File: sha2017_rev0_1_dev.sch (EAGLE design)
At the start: 87 parts, among them IC1 AP7215, IC2 LM1117, IC3 CP210X_USB_UART, IC4 ESP32WROOM32, Q1 MMBT2222A, Q2 MMBT2222A, Q3 SI1304 BDL, SW100 MCMT5-F-V, X701 2908-05WB-MG

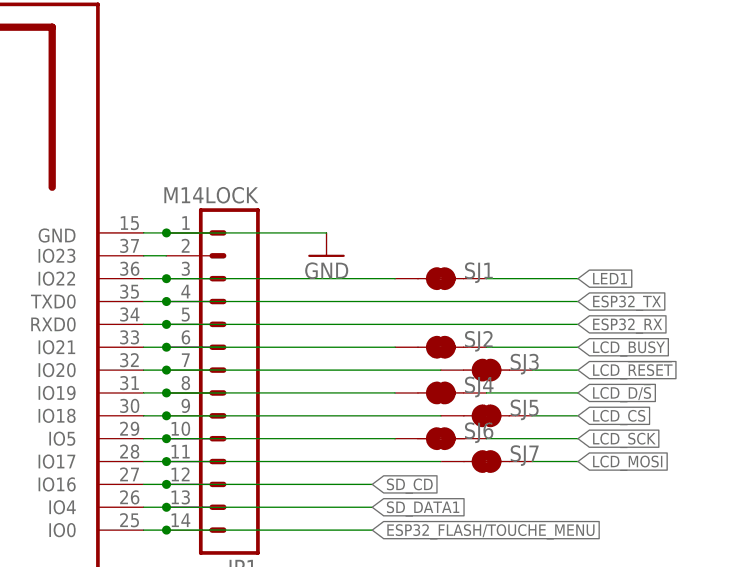
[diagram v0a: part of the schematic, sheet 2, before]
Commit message: Swapped NC and IO23
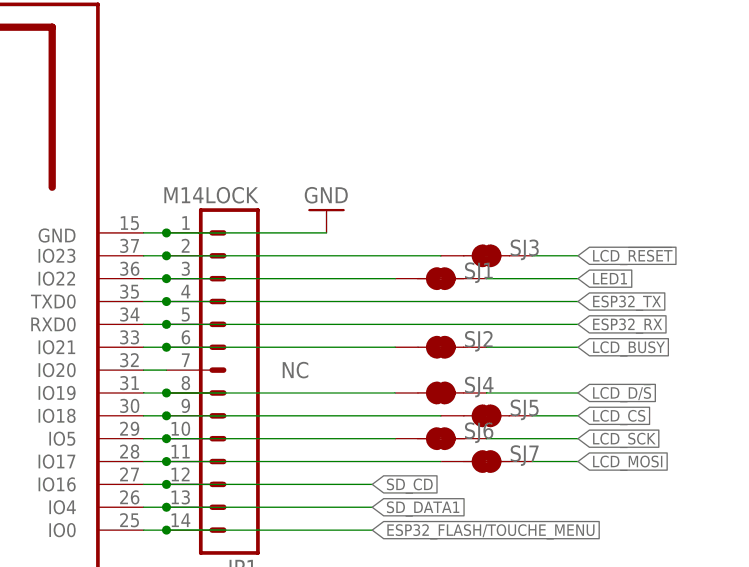
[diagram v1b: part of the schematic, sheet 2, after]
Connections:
- removed net N$18: IC4.IO20, JP1.7, SJ3.1
- new net N$2: IC4.IO23, JP1.2, SJ3.1
- net N$15: now also IC4.IO20, JP1.7; no longer IC4.IO23, JP1.2
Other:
- note added: "NC"
- moved on the sheet: SJ3
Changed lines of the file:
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@@
 <plain>
 <text x="152.4" y="218.44" size="6.4516" layer="94">MCU/WIFI</text>
+<text x="233.68" y="137.16" size="1.778" layer="95" align="center-left">NC</text>
 </plain>
 <instances>
@@
 <attribute name="NAME" x="132.08" y="124.46" size="1.778" layer="95"/>
 </instance>
-<instance part="SJ3" gate="G$1" x="256.54" y="137.16" smashed="yes">
-<attribute name="NAME" x="259.08" y="137.16" size="1.778" layer="95"/>
+<instance part="SJ3" gate="G$1" x="256.54" y="149.86" smashed="yes">
+<attribute name="NAME" x="259.08" y="149.86" size="1.778" layer="95"/>
 </instance>
 <instance part="SJ5" gate="G$1" x="256.54" y="132.08" smashed="yes">
@@
 <instance part="JP1" gate="G$1" x="231.14" y="134.62" rot="R180"/>
 <instance part="GND2" gate="1" x="177.8" y="91.44" rot="MR0"/>
-<instance part="GND3" gate="1" x="238.76" y="149.86" rot="MR0"/>
+<instance part="GND3" gate="1" x="238.76" y="154.94" rot="MR180"/>
 <instance part="JP3" gate="G$1" x="144.78" y="137.16"/>
 </instances>
@@
 </segment>
 </net>
-<net name="N$18" class="0">
-<segment>
-<pinref part="IC4" gate="G$1" pin="IO20"/>
-<wire x1="218.44" y1="137.16" x2="220.98" y2="137.16" width="0.1524" layer="91"/>
-<pinref part="JP1" gate="G$1" pin="7"/>
-<pinref part="SJ3" gate="G$1" pin="1"/>
-<wire x1="220.98" y1="137.16" x2="251.46" y2="137.16" width="0.1524" layer="91"/>
-<junction x="220.98" y="137.16"/>
-</segment>
-</net>
 <net name="BT_LEFT" class="0">
 <segment>
@@
 <net name="LCD_!RESET" class="0">
 <segment>
-<label x="266.7" y="137.16" size="1.27" layer="95" xref="yes"/>
+<label x="266.7" y="149.86" size="1.27" layer="95" xref="yes"/>
 <pinref part="SJ3" gate="G$1" pin="2"/>
-<wire x1="261.62" y1="137.16" x2="266.7" y2="137.16" width="0.1524" layer="91"/>
+<wire x1="261.62" y1="149.86" x2="266.7" y2="149.86" width="0.1524" layer="91"/>
 </segment>
 </net>
@@
 </segment>
 </net>
+<net name="N$2" class="0">
+<segment>
+<pinref part="SJ3" gate="G$1" pin="1"/>
+<pinref part="JP1" gate="G$1" pin="2"/>
+<wire x1="251.46" y1="149.86" x2="220.98" y2="149.86" width="0.1524" layer="91"/>
+<pinref part="IC4" gate="G$1" pin="IO23"/>
+<wire x1="218.44" y1="149.86" x2="220.98" y2="149.86" width="0.1524" layer="91"/>
+<junction x="220.98" y="149.86"/>
+</segment>
+</net>
 <net name="N$15" class="0">
 <segment>
-<pinref part="IC4" gate="G$1" pin="IO23"/>
-<pinref part="JP1" gate="G$1" pin="2"/>
-<wire x1="218.44" y1="149.86" x2="220.98" y2="149.86" width="0.1524" layer="91"/>
-</segment>
-</net>
+<pinref part="IC4" gate="G$1" pin="IO20"/>
+<pinref part="JP1" gate="G$1" pin="7"/>
+<wire x1="218.44" y1="137.16" x2="220.98" y2="137.16" width="0.1524" layer="91"/>
+</segment>
+</net>
